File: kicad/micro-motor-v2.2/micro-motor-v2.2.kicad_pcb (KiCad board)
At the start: 4 copper layers, 35 x 20 mm, 80 parts, among them J101 SUPPLY, J102 SW, J103 Hall, J104 Encoder, J105 CAN2, J106 Motor, J107 CAN, J301 USB, J302 UART, J303 SWD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

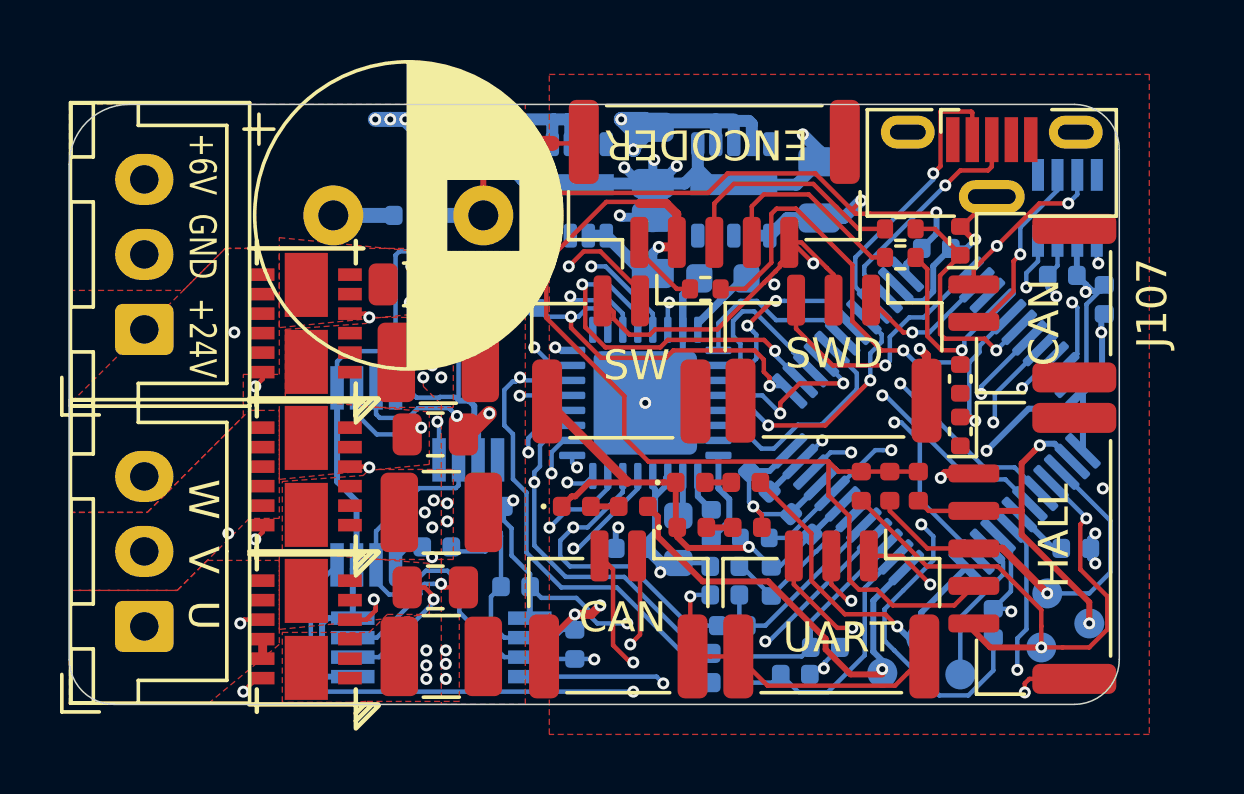
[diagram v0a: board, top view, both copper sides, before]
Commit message: solved most critical DRC issues
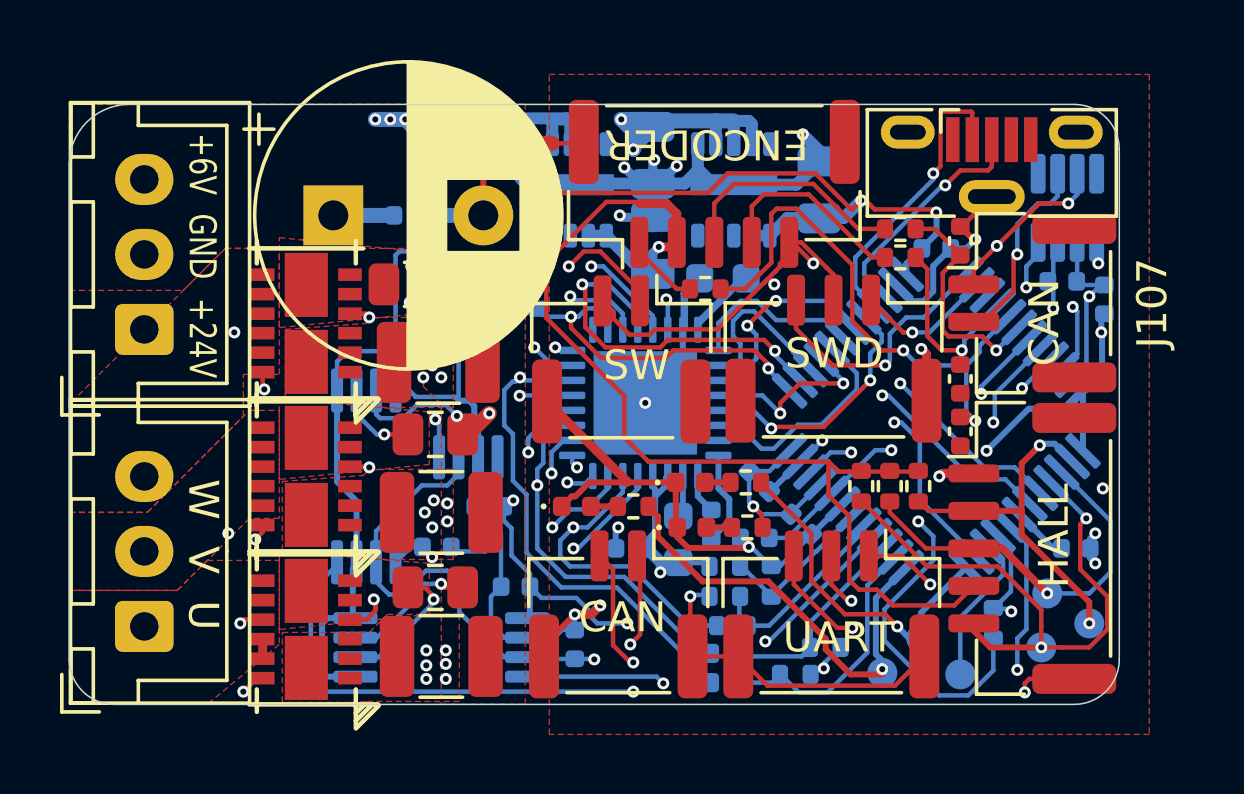
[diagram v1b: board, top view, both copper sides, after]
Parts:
- moved C201 0.20 mm to (183.1, 105.9)
- moved R103 0.05 mm to (171.8, 116.4)
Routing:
- net Net-(Q403-G1): track 11.6 -> 11.1 mm
